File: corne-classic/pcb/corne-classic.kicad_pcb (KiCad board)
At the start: 2 copper layers, 133.8 x 92.2 mm, 98 parts, among them J1 MJ-4PP-9, J2 OLED, J3 LED, P1 i2c-pin, P2 i2c-pin, SW1 SW_PUSH, SW10 SW_PUSH, SW11 SW_PUSH, SW12 SW_PUSH, SW13 SW_PUSH, SW14 SW_PUSH, SW15 SW_PUSH, SW16 SW_PUSH, SW17 SW_PUSH, SW18 SW_PUSH, SW19 SW_PUSH, SW2 SW_PUSH, SW20 SW_PUSH, SW21 SW_PUSH, SW3 SW_PUSH, SW4 SW_PUSH, SW5 SW_PUSH, SW6 SW_PUSH, SW7 SW_PUSH, SW8 SW_PUSH, SW9 SW_PUSH, U1 ProMicro

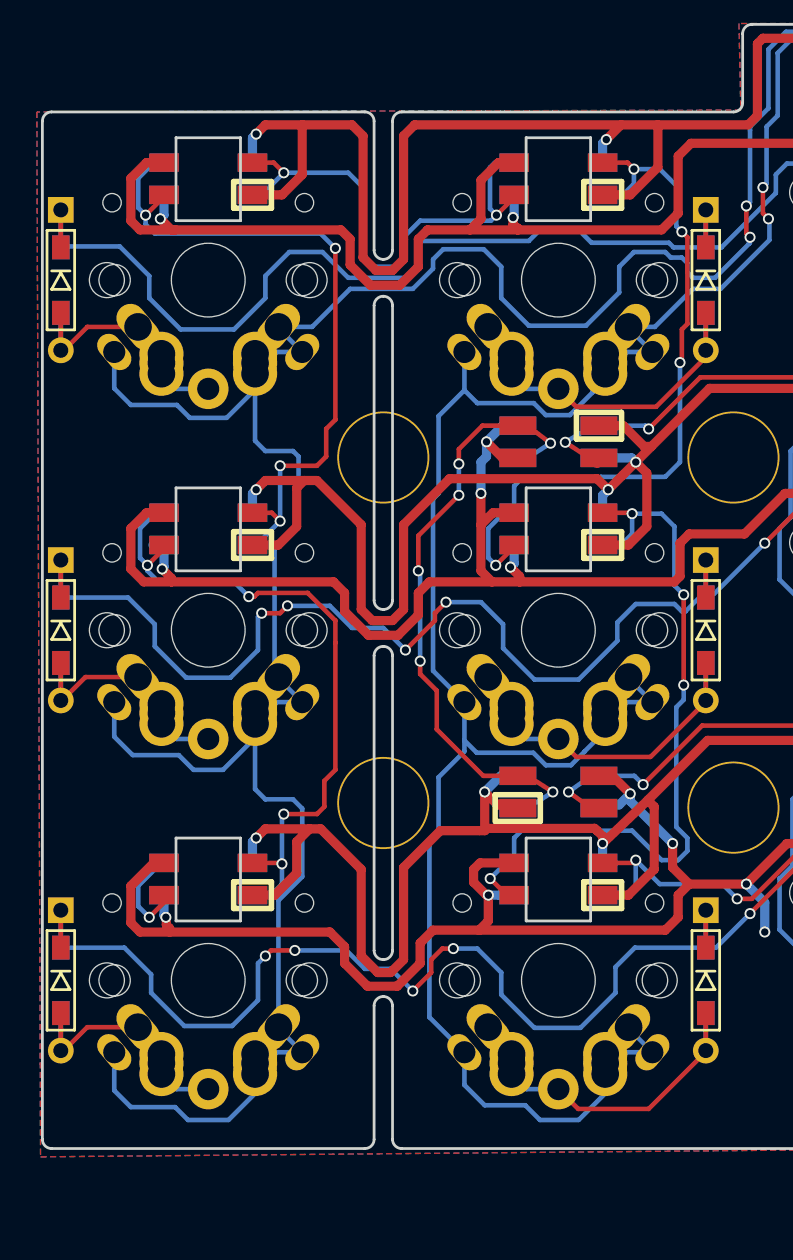
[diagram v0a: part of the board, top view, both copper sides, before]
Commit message: removed breaking off feature
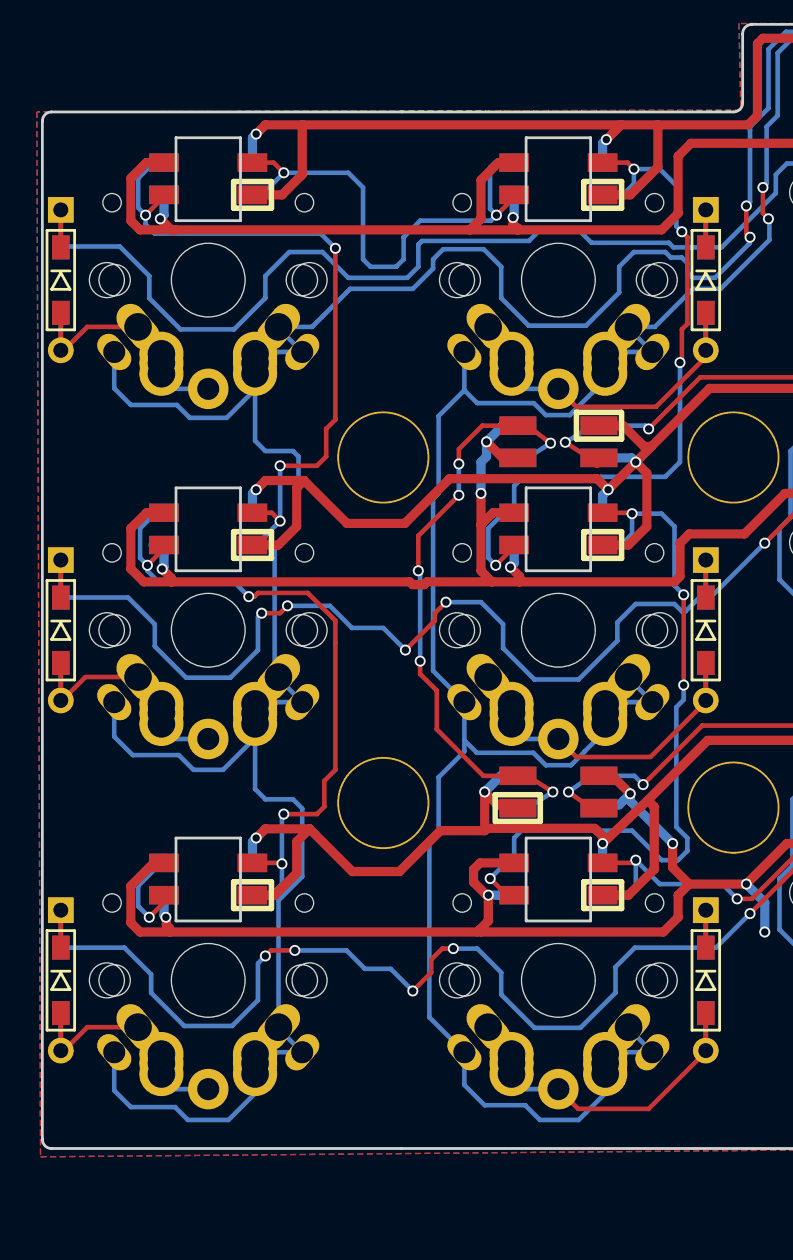
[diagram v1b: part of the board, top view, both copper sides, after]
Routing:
- net VCC: track 759.0 -> 724.7 mm
- net GND: track 797.9 -> 786.6 mm
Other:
- outline, holes or cut-outs redrawn

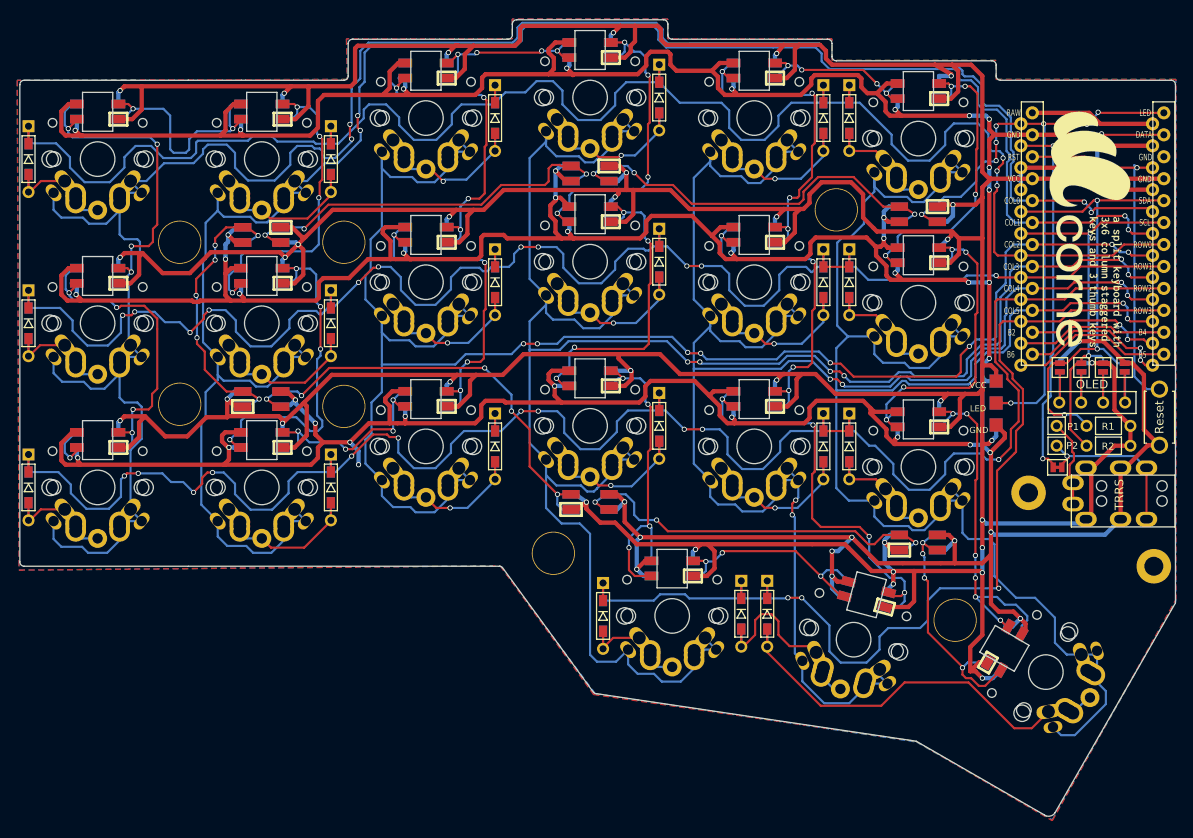
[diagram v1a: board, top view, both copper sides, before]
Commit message: added gateron low profile support
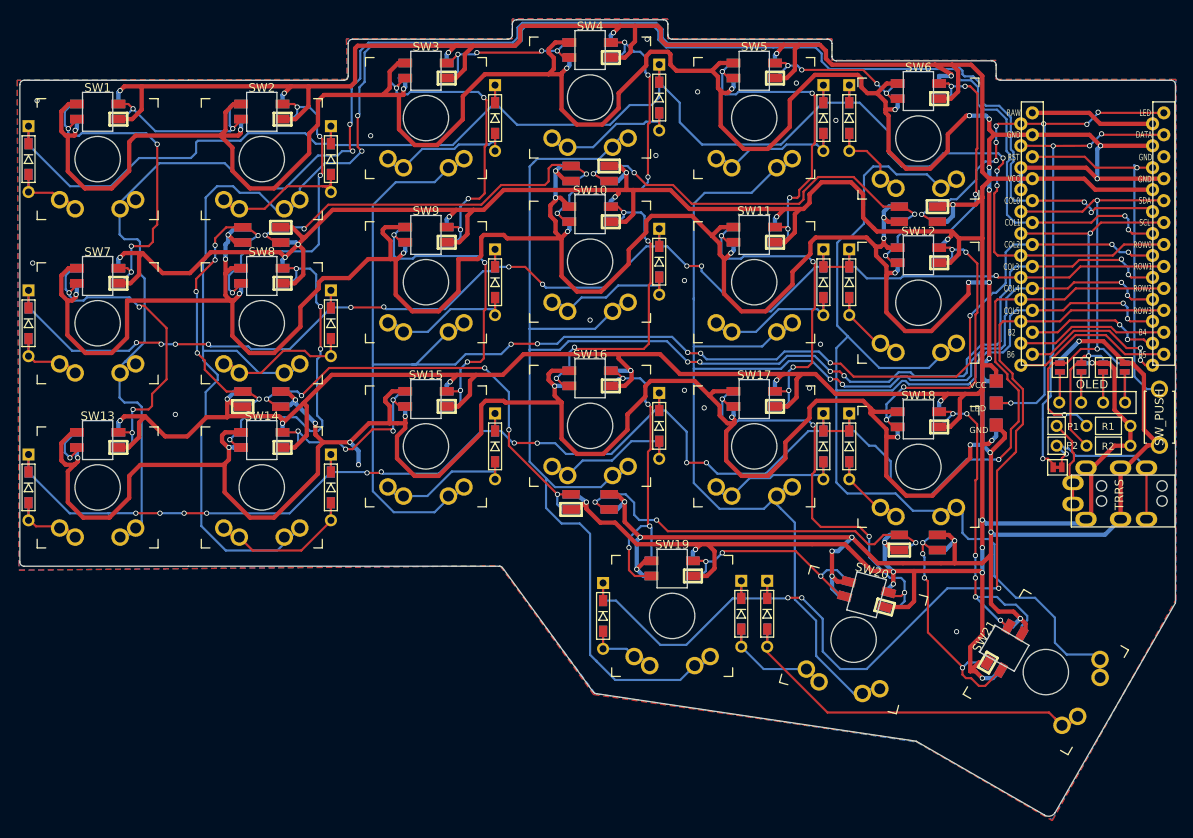
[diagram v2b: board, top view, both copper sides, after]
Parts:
- removed ? (x9): , kbd:LEGO_HOLE
- removed G*** (x2): LOGO, kbd:corne
- RSW1: value Reset -> SW_PUSH
- SW1, SW10, SW11, SW12, SW13, SW14, SW15, SW16, SW17, SW18, SW19, SW2, SW20, SW3, SW4, SW5, SW6, SW7, SW8, SW9: footprint kbd:MX_ALPS_PG1350_noLed -> gateron:Gateron_low_profile_noled_reversible_bighole
- SW21: footprint kbd:MX_ALPS_PG1350_noLed_1.75u -> gateron:Gateron_low_profile_noled_reversible_bighole
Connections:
- J1 pad B: Net-(J1-PadB) -> Net-(P2-Pin_1)
- L19 pad 1: Net-(L13-Pad1) -> unconnected-(L19-DOUT-Pad1)
- L27 pad 3: Net-(L21-Pad3) -> Net-(L27-DIN)
- P2 pad 1: Net-(J1-PadB) -> Net-(P2-Pin_1)
- U1 pad 11: Net-(U1-Pad11) -> unconnected-(U1-B4-Pad11)
- U1 pad 12: Net-(U1-Pad12) -> unconnected-(U1-B5-Pad12)
- U1 pad 13: Net-(U1-Pad13) -> unconnected-(U1-B6-Pad13)
- U1 pad 14: Net-(U1-Pad14) -> unconnected-(U1-B2-Pad14)
- U1 pad 24: Net-(U1-Pad24) -> unconnected-(U1-RAW-Pad24)
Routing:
- net GND: track 786.6 -> 949.3 mm, vias 49 -> 65
- net col0: track 245.7 -> 205.5 mm
- net col5: track 187.0 -> 160.7 mm
- net col4: track 194.3 -> 169.4 mm, vias 6 -> 4
- net col2: track 197.5 -> 175.2 mm
- net col3: track 225.1 -> 203.8 mm
- net row1: track 191.7 -> 172.7 mm
- net unconnected-(U1-B5-Pad12): track 0.00 -> 18.9 mm
- net Net-(U1-Pad12): track 18.9 -> 0.00 mm
- net unconnected-(U1-B4-Pad11): track 0.00 -> 17.6 mm
- net Net-(U1-Pad11): track 17.6 -> 0.00 mm
- net unconnected-(U1-B6-Pad13): track 0.00 -> 17.5 mm, vias 0 -> 2
- net Net-(U1-Pad13): track 17.5 -> 0.00 mm, vias 2 -> 0
- net Net-(P2-Pin_1): track 0.00 -> 17.3 mm
- net unconnected-(U1-B2-Pad14): track 0.00 -> 16.0 mm, vias 0 -> 2
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
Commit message: added gateron lp mod text
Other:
- board text added: "Corne Classic v2.0 PCB designed by foostan Gateron low-profile mod"
- board text removed: "Corne Classic v2.0 PCB designed by foostan"
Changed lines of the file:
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@@
     (effects (font (size 0.7 0.7) (thickness 0.125)))
   )
-  (gr_text "Corne Classic v2.0\nPCB designed by foostan" (at 119.4 121.5) (layer "B.Mask")
+  (gr_text "Corne Classic v2.0\nPCB designed by foostan\nGateron low-profile mod" (at 118.872 120.142) (layer "B.Mask")
     (effects (font (size 1 1) (thickness 0.125)) (justify left mirror))
   )
-  (gr_text "Corne Classic v2.0\nPCB designed by foostan" (at 100.1 121.5) (layer "F.Mask")
+  (gr_text "Corne Classic v2.0\nPCB designed by foostan\nGateron low-profile mod" (at 99.822 119.888) (layer "F.Mask")
     (effects (font (size 1 1) (thickness 0.125)) (justify left))
   )

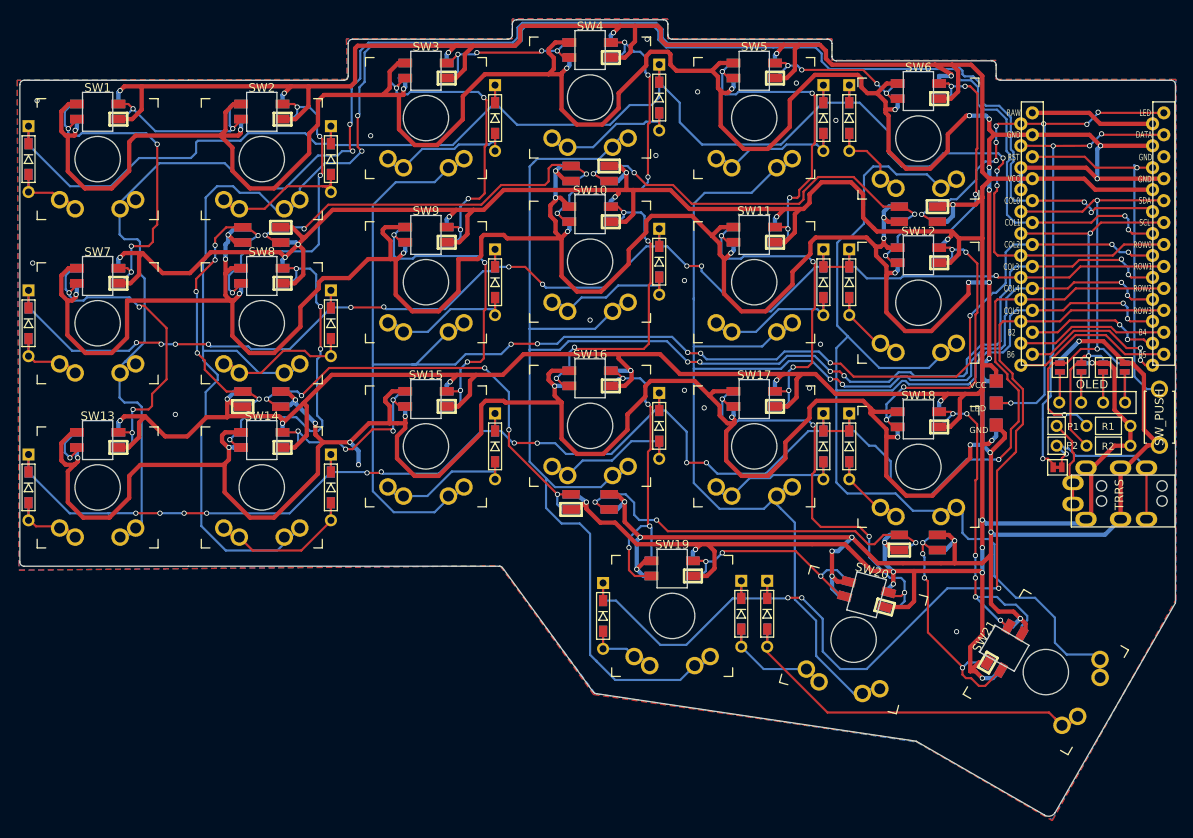
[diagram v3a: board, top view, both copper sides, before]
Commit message: re-added missing parts (holes and silkscreen)
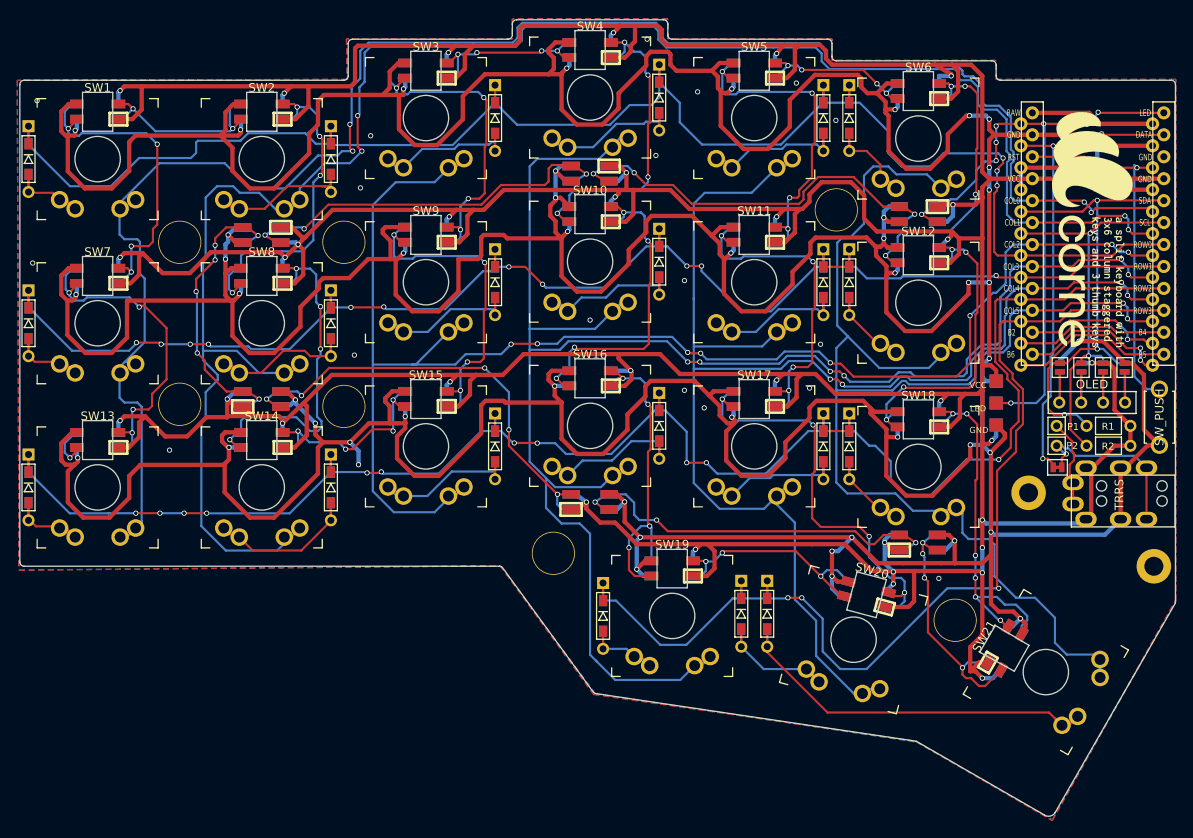
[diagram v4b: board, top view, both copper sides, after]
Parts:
- added ?: , , F.Cu at (79.5, 86.8)
- added ?: , , F.Cu at (177.8, 115.8)
- added ?: , , F.Cu at (98.5, 86.8)
- added ?: , , F.Cu at (79.5, 105.5)
- added ?: , , F.Cu at (155.5, 83.0)
- added ?: , , F.Cu at (192.3, 124.3)
- added ?: , , F.Cu at (98.5, 105.8)
- added ?: , , F.Cu at (122.8, 122.8)
- added ?: , , F.Cu at (169.3, 130.5)
- added G***: LOGO, kbd:corne, F.Cu at (185.0, 85.4)
- added G***: LOGO, kbd:corne, B.Cu at (183.9, 85.4)
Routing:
- net Net-(L14-DOUT): track 39.4 -> 38.7 mm
- net GND: vias 65 -> 67
